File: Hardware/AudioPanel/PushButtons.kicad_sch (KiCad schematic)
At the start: 36 parts, among them CN3 4x 10nF, CN4 4x 10nF, CN5 4x 10nF, U10 74HC14, U11 74HC14, U16 MCP23017_ML

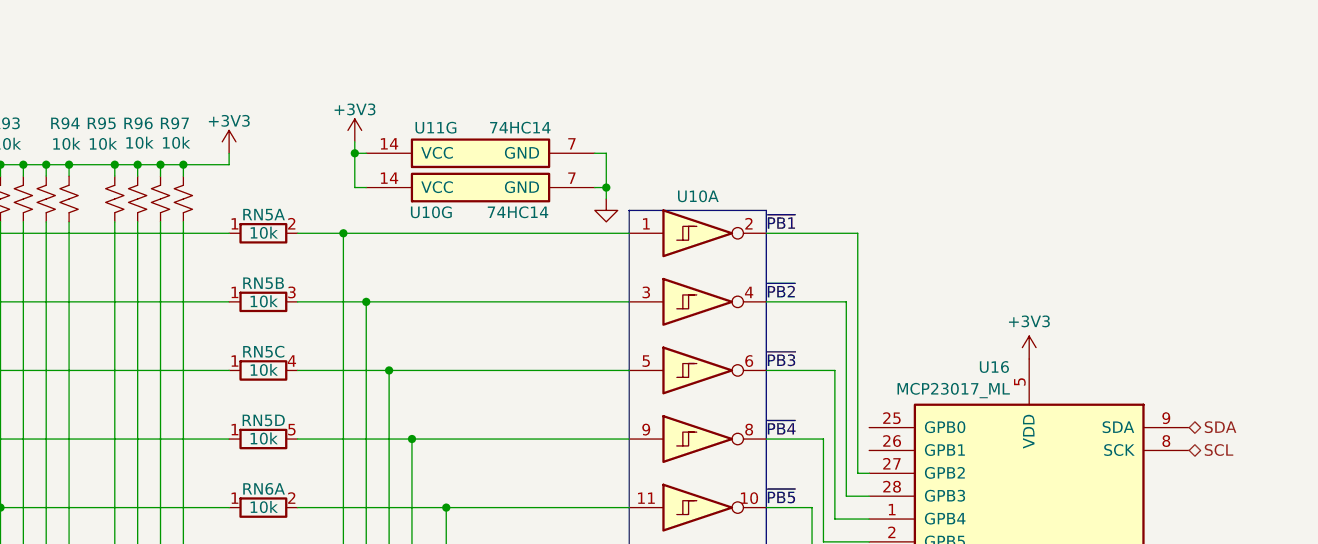
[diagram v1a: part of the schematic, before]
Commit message: Added headphone and speaker jack interfaces
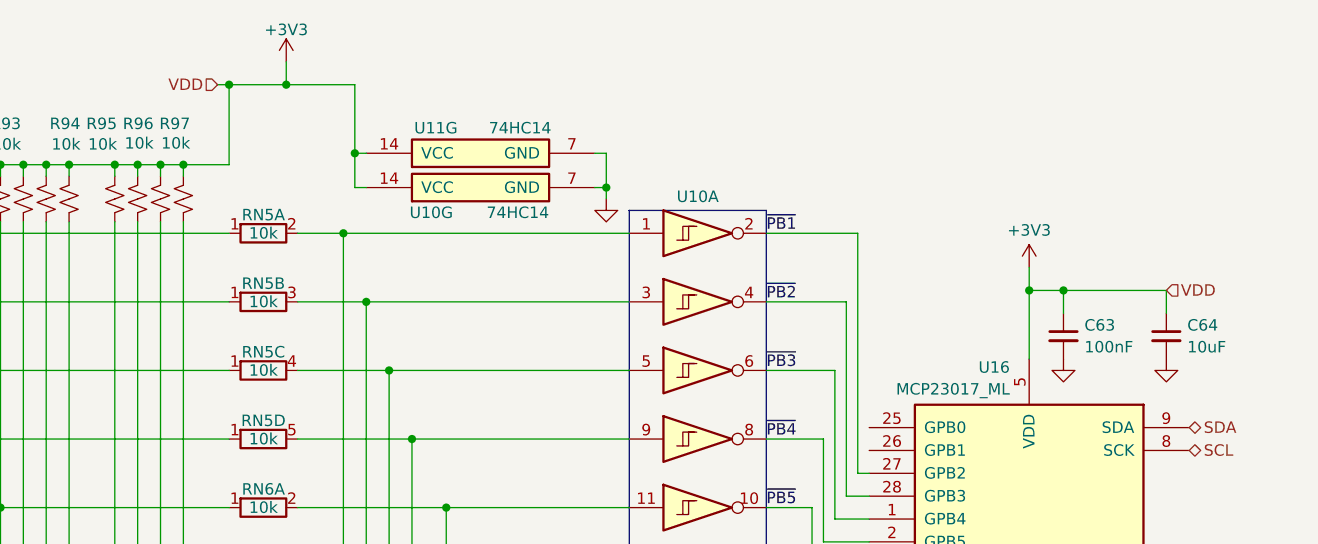
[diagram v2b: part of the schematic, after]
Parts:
- added C63: 100nF, symbol Device:C_Small
- added C64: 10uF, symbol Device:C_Small
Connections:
- net +3V3: now also C63.1, C64.1
- net GND: now also C63.2, C64.2

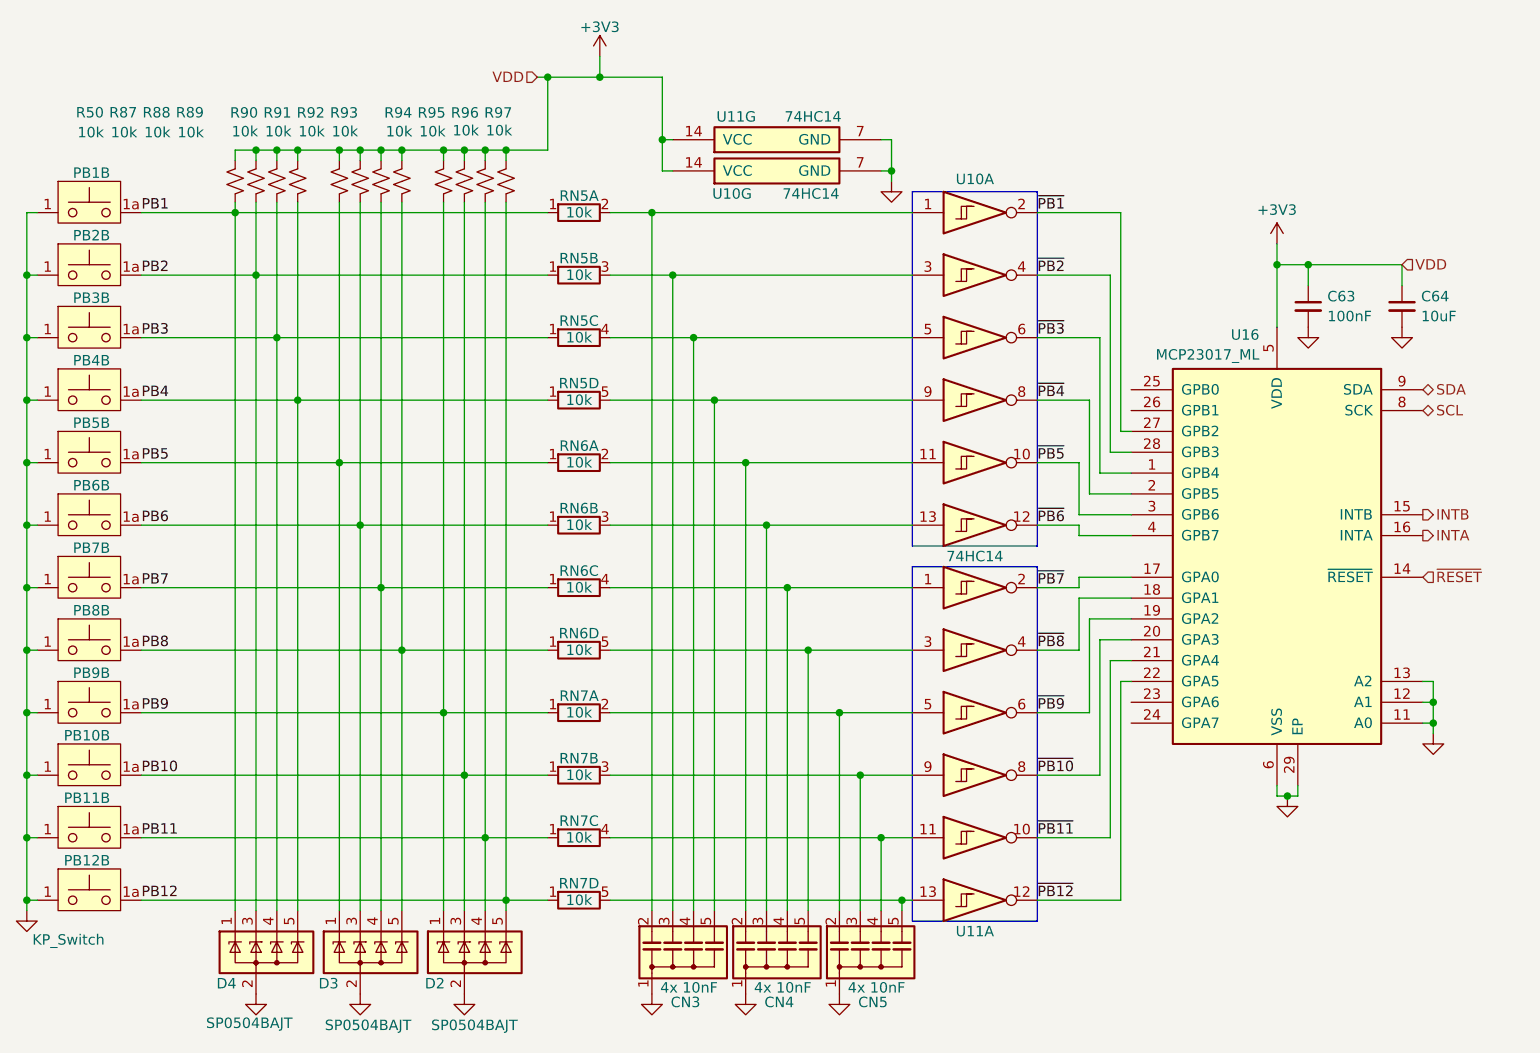
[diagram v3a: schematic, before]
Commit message: Realized that I need to rethink how I'm going to mix the radio audio with the stereo audio
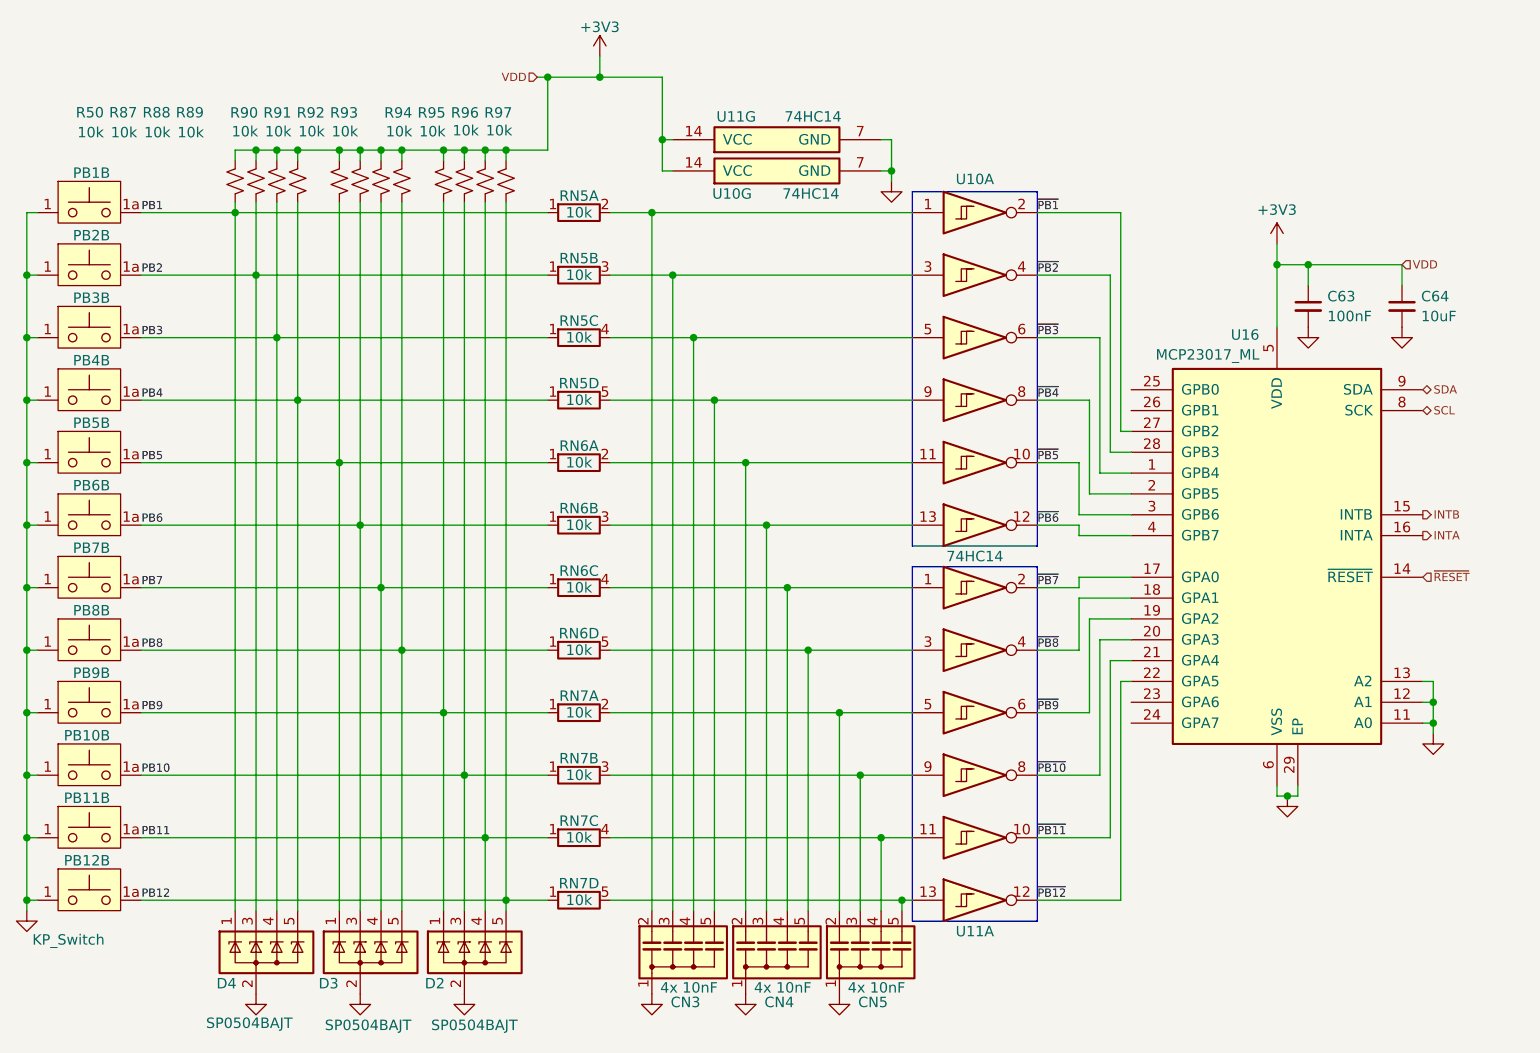
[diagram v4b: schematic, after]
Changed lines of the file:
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@@
 		(effects
 			(font
-				(size 1.27 1.27)
+				(size 1 1)
 			)
 			(justify left bottom)
@@
 		(effects
 			(font
-				(size 1.27 1.27)
+				(size 1 1)
 			)
 			(justify left bottom)
@@
 		(effects
 			(font
-				(size 1.27 1.27)
+				(size 1 1)
 			)
 			(justify left bottom)
@@
 		(effects
 			(font
-				(size 1.27 1.27)
+				(size 1 1)
 			)
 			(justify left bottom)
@@
 		(effects
 			(font
-				(size 1.27 1.27)
+				(size 1 1)
 			)
 			(justify left bottom)
@@
 		(effects
 			(font
-				(size 1.27 1.27)
+				(size 1 1)
 			)
 			(justify left bottom)
@@
 		(effects
 			(font
-				(size 1.27 1.27)
+				(size 1 1)
 			)
 			(justify left bottom)
@@
 		(effects
 			(font
-				(size 1.27 1.27)
+				(size 1 1)
 			)
 			(justify left bottom)
@@
 		(effects
 			(font
-				(size 1.27 1.27)
+				(size 1 1)
 			)
 			(justify left bottom)
@@
 		(effects
 			(font
-				(size 1.27 1.27)
+				(size 1 1)
 			)
 			(justify left bottom)
@@
 		(effects
 			(font
-				(size 1.27 1.27)
+				(size 1 1)
 			)
 			(justify left bottom)
@@
 		(effects
 			(font
-				(size 1.27 1.27)
+				(size 1 1)
 			)
 			(justify left bottom)
@@
 		(effects
 			(font
-				(size 1.27 1.27)
+				(size 1 1)
 			)
 			(justify left bottom)
@@
 		(effects
 			(font
-				(size 1.27 1.27)
+				(size 1 1)
 			)
 			(justify left bottom)
@@
 		(effects
 			(font
-				(size 1.27 1.27)
+				(size 1 1)
 			)
 			(justify left bottom)
@@
 		(effects
 			(font
-				(size 1.27 1.27)
+				(size 1 1)
 			)
 			(justify left bottom)
@@
 		(effects
 			(font
-				(size 1.27 1.27)
+				(size 1 1)
 			)
 			(justify left bottom)
@@
 		(effects
 			(font
-				(size 1.27 1.27)
+				(size 1 1)
 			)
 			(justify left bottom)
@@
 		(effects
 			(font
-				(size 1.27 1.27)
+				(size 1 1)
 			)
 			(justify left bottom)
@@
 		(effects
 			(font
-				(size 1.27 1.27)
+				(size 1 1)
 			)
 			(justify left bottom)
@@
 		(effects
 			(font
-				(size 1.27 1.27)
+				(size 1 1)
 			)
 			(justify left bottom)
@@
 		(effects
 			(font
-				(size 1.27 1.27)
+				(size 1 1)
 			)
 			(justify left bottom)
@@
 		(effects
 			(font
-				(size 1.27 1.27)
+				(size 1 1)
 			)
 			(justify left bottom)
@@
 		(effects
 			(font
-				(size 1.27 1.27)
+				(size 1 1)
 			)
 			(justify left bottom)
@@
 		(effects
 			(font
-				(size 1.27 1.27)
+				(size 1 1)
 				(color 105 14 0 1)
 			)
@@
 		(effects
 			(font
-				(size 1.27 1.27)
+				(size 1 1)
 				(color 105 14 0 1)
 			)
@@
 		(effects
 			(font
-				(size 1.27 1.27)
+				(size 1 1)
 				(color 105 14 0 1)
 			)
@@
 		(effects
 			(font
-				(size 1.27 1.27)
+				(size 1 1)
 				(color 105 14 0 1)
 			)
@@
 		(effects
 			(font
-				(size 1.27 1.27)
+				(size 1 1)
 			)
 			(justify left)
@@
 		(effects
 			(font
-				(size 1.27 1.27)
+				(size 1 1)
 			)
 			(justify right)
@@
 		(effects
 			(font
-				(size 1.27 1.27)
-				(color 105 14 0 1)
-			)
+				(size 1 1)
+				(color 105 14 0 1)
+			)

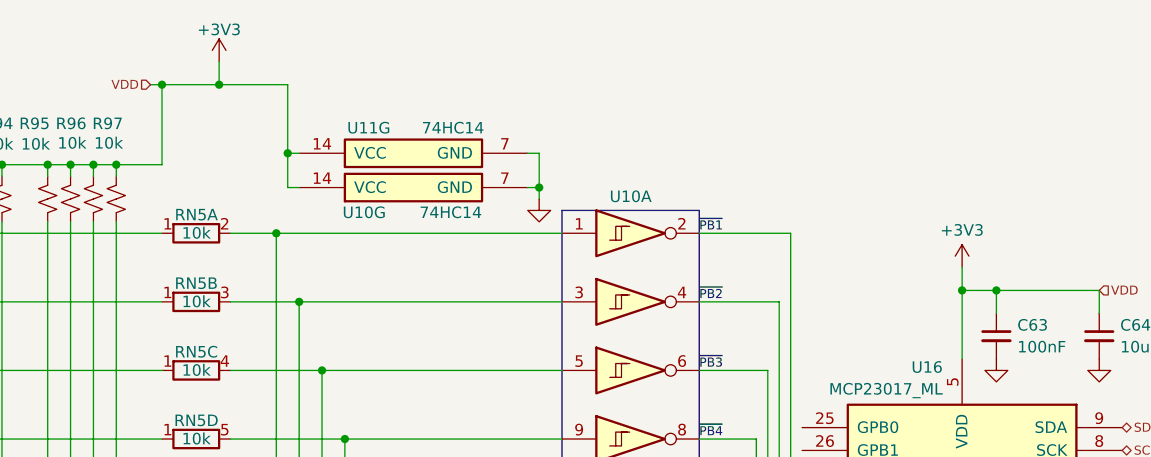
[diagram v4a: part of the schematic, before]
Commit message: Cleaned up sheet voltage inputs
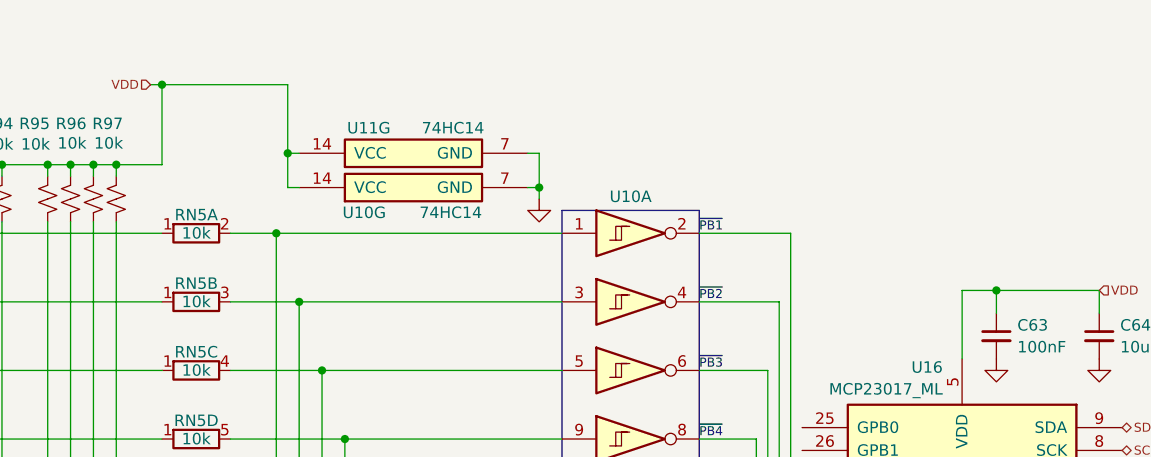
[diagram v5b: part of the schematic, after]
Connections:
- net +3V3 renamed VDD
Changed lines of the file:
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@@
 	)
 	(junction
-		(at 118.11 43.18)
-		(diameter 0)
-		(color 0 0 0 0)
-	)
-	(junction
 		(at 138.43 97.79)
 		(diameter 0)
@@
 	)
 	(junction
-		(at 200.66 66.04)
-		(diameter 0)
-		(color 0 0 0 0)
-	)
-	(junction
 		(at 48.26 105.41)
 		(diameter 0)
@@
 	(wire
 		(pts
-			(xy 118.11 40.64) (xy 118.11 43.18)
-		)
-		(stroke
-			(width 0)
-			(type default)
-		)
-	)
-	(wire
-		(pts
 			(xy 81.28 58.42) (xy 81.28 82.55)
 		)
@@
 	(wire
 		(pts
-			(xy 200.66 63.5) (xy 200.66 66.04)
-		)
-		(stroke
-			(width 0)
-			(type default)
-		)
-	)
-	(wire
-		(pts
 			(xy 132.08 82.55) (xy 132.08 144.78)
 		)
@@
 	(wire
 		(pts
-			(xy 118.11 43.18) (xy 111.76 43.18)
+			(xy 111.76 43.18) (xy 125.73 43.18)
 		)
 		(stroke
@@
 	(wire
 		(pts
-			(xy 125.73 43.18) (xy 118.11 43.18)
-		)
-		(stroke
-			(width 0)
-			(type default)
-		)
-	)
-	(wire
-		(pts
 			(xy 78.74 58.42) (xy 78.74 74.93)
 		)
@@
 	)
 	(symbol
-		(lib_id "power:+3V3")
-		(at 200.66 63.5 0)
-		(unit 1)
-		(exclude_from_sim no)
-		(in_bom yes)
-		(on_board yes)
-		(dnp no)
-		(fields_autoplaced yes)
-		(property "Reference" "#PWR0114"
-			(at 200.66 67.31 0)
-			(effects
-				(font
-					(size 1.27 1.27)
-				)
-				(hide yes)
-			)
-		)
-		(property "Value" "+3V3"
-			(at 200.66 59.3669 0)
-			(effects
-				(font
-					(size 1.27 1.27)
-				)
-			)
-		)
-		(property "Footprint" ""
-			(at 200.66 63.5 0)
-			(effects
-				(font
-					(size 1.27 1.27)
-				)
-				(hide yes)
-			)
-		)
-		(property "Datasheet" ""
-			(at 200.66 63.5 0)
-			(effects
-				(font
-					(size 1.27 1.27)
-				)
-				(hide yes)
-			)
-		)
-		(property "Description" "Power symbol creates a global label with name \"+3V3\""
-			(at 200.66 63.5 0)
-			(effects
-				(font
-					(size 1.27 1.27)
-				)
-				(hide yes)
-			)
-		)
-		(pin "1"
-		)
-		(instances
-			(project "PilotAudioPanel"
-				(path "/2de36a1b-eee5-458c-8325-256a7162eff5/a5cce8a2-fa1f-45df-8605-c295d18be7f1/292d3d4d-f17c-45e8-bc8b-f5444b88eee7"
-					(reference "#PWR0114")
-					(unit 1)
-				)
-			)
-		)
-	)
-	(symbol
 		(lib_id "Power_Protection:SP0504BAJT")
 		(at 101.6 149.86 0)
@@
 					(unit 1)
 				)
-			)
-		)
-	)
-	(symbol
-		(lib_id "power:+3V3")
-		(at 118.11 40.64 0)
-		(unit 1)
-		(exclude_from_sim no)
-		(in_bom yes)
-		(on_board yes)
-		(dnp no)
-		(property "Reference" "#PWR054"
-			(at 118.11 44.45 0)
-			(effects
-				(font
-					(size 1.27 1.27)
-				)
-				(hide yes)
-			)
-		)
-		(property "Value" "+3V3"
-			(at 118.11 37.084 0)
-			(effects
-				(font
-					(size 1.27 1.27)
-				)
-			)
-		)
-		(property "Footprint" ""
-			(at 118.11 40.64 0)
-			(effects
-				(font
-					(size 1.27 1.27)
-				)
-				(hide yes)
-			)
-		)
-		(property "Datasheet" ""
-			(at 118.11 40.64 0)
-			(effects
-				(font
-					(size 1.27 1.27)
-				)
-				(hide yes)
-			)
-		)
-		(property "Description" "Power symbol creates a global label with name \"+3V3\""
-			(at 118.11 40.64 0)
-			(effects
-				(font
-					(size 1.27 1.27)
-				)
-				(hide yes)
-			)
-		)
-		(pin "1"
-		)
-		(instances
-			(project "PilotAudioPanel"
-				(path "/2de36a1b-eee5-458c-8325-256a7162eff5/a5cce8a2-fa1f-45df-8605-c295d18be7f1/292d3d4d-f17c-45e8-bc8b-f5444b88eee7"
-					(reference "#PWR054")
-					(unit 1)
-				)
